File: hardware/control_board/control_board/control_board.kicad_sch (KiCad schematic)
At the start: 5 parts, among them J1 Conn_02x08_Counter_Clockwise, J3 USB_B

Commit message: feat：EEPROM原理图
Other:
- moved on the sheet: D2
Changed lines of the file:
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@@
 	(wire
 		(pts
-			(xy 55.88 29.21) (xy 55.88 30.48)
+			(xy 45.72 29.21) (xy 45.72 30.48)
 		)
 		(stroke
@@
 	(wire
 		(pts
-			(xy 55.88 55.88) (xy 55.88 58.42)
+			(xy 45.72 55.88) (xy 45.72 58.42)
 		)
 		(stroke
@@
 	(wire
 		(pts
-			(xy 27.94 43.18) (xy 43.18 43.18)
+			(xy 17.78 43.18) (xy 33.02 43.18)
 		)
 		(stroke
@@
 	(wire
 		(pts
-			(xy 68.58 43.18) (xy 82.55 43.18)
+			(xy 58.42 43.18) (xy 72.39 43.18)
 		)
 		(stroke
@@
 	)
 	(label "USB_D.USB_D+"
-		(at 27.94 43.18 0)
+		(at 17.78 43.18 0)
 		(effects
 			(font
@@
 	)
 	(label "USB_D.USB_D-"
-		(at 68.58 43.18 0)
+		(at 58.42 43.18 0)
 		(effects
 			(font
@@
 	(symbol
 		(lib_id "power:VBUS")
-		(at 55.88 29.21 0)
+		(at 45.72 29.21 0)
 		(unit 1)
 		(body_style 1)
@@
 		(fields_autoplaced yes)
 		(property "Reference" "#PWR021"
-			(at 55.88 33.02 0)
+			(at 45.72 33.02 0)
 			(hide yes)
 			(show_name no)
@@
 		)
 		(property "Value" "VBUS"
-			(at 55.88 24.13 0)
+			(at 45.72 24.13 0)
 			(show_name no)
 			(do_not_autoplace no)
@@
 		)
 		(property "Footprint" ""
-			(at 55.88 29.21 0)
+			(at 45.72 29.21 0)
 			(hide yes)
 			(show_name no)
@@
 		)
 		(property "Datasheet" ""
-			(at 55.88 29.21 0)
+			(at 45.72 29.21 0)
 			(hide yes)
 			(show_name no)
@@
 		)
 		(property "Description" "Power symbol creates a global label with name \"VBUS\""
-			(at 55.88 29.21 0)
+			(at 45.72 29.21 0)
 			(hide yes)
 			(show_name no)
@@
 	(symbol
 		(lib_id "Power_Protection:PRTR5V0U2X")
-		(at 55.88 43.18 0)
+		(at 45.72 43.18 0)
 		(unit 1)
 		(body_style 1)
@@
 		(dnp no)
 		(property "Reference" "D2"
-			(at 65.532 30.988 0)
+			(at 55.372 30.988 0)
 			(show_name no)
 			(do_not_autoplace no)
@@
 		)
 		(property "Value" "PRTR5V0U2X"
-			(at 65.532 33.528 0)
+			(at 55.372 33.528 0)
 			(show_name no)
 			(do_not_autoplace no)
@@
 		)
 		(property "Footprint" "Package_TO_SOT_SMD:SOT-143"
-			(at 57.404 43.18 0)
+			(at 47.244 43.18 0)
 			(hide yes)
 			(show_name no)
@@
 		)
 		(property "Datasheet" "https://assets.nexperia.com/documents/data-sheet/PRTR5V0U2X.pdf"
-			(at 57.404 43.18 0)
+			(at 47.244 43.18 0)
 			(hide yes)
 			(show_name no)
@@
 		)
 		(property "Description" "Ultra low capacitance double rail-to-rail ESD protection diode, SOT-143"
-			(at 55.88 43.18 0)
+			(at 45.72 43.18 0)
 			(hide yes)
 			(show_name no)
@@
 		)
 		(property "KLC_S3.3" ""
-			(at 55.88 43.18 0)
+			(at 45.72 43.18 0)
 			(hide yes)
 			(show_name no)
@@
 		)
 		(property "KLC_S4.1" ""
-			(at 55.88 43.18 0)
+			(at 45.72 43.18 0)
 			(hide yes)
 			(show_name no)
@@
 	(symbol
 		(lib_id "power:GND")
-		(at 55.88 58.42 0)
+		(at 45.72 58.42 0)
 		(unit 1)
 		(body_style 1)
@@
 		(fields_autoplaced yes)
 		(property "Reference" "#PWR020"
-			(at 55.88 64.77 0)
+			(at 45.72 64.77 0)
 			(hide yes)
 			(show_name no)
@@
 		)
 		(property "Value" "GND"
-			(at 55.88 63.5 0)
+			(at 45.72 63.5 0)
 			(show_name no)
 			(do_not_autoplace no)
@@
 		)
 		(property "Footprint" ""
-			(at 55.88 58.42 0)
+			(at 45.72 58.42 0)
 			(hide yes)
 			(show_name no)
@@
 		)
 		(property "Datasheet" ""
-			(at 55.88 58.42 0)
+			(at 45.72 58.42 0)
 			(hide yes)
 			(show_name no)
@@
 		)
 		(property "Description" "Power symbol creates a global label with name \"GND\" , ground"
-			(at 55.88 58.42 0)
-			(hide yes)
-			(show_name no)
+			(at 45.72 58.42 0)
+			(hide yes)
+			(show_name no)

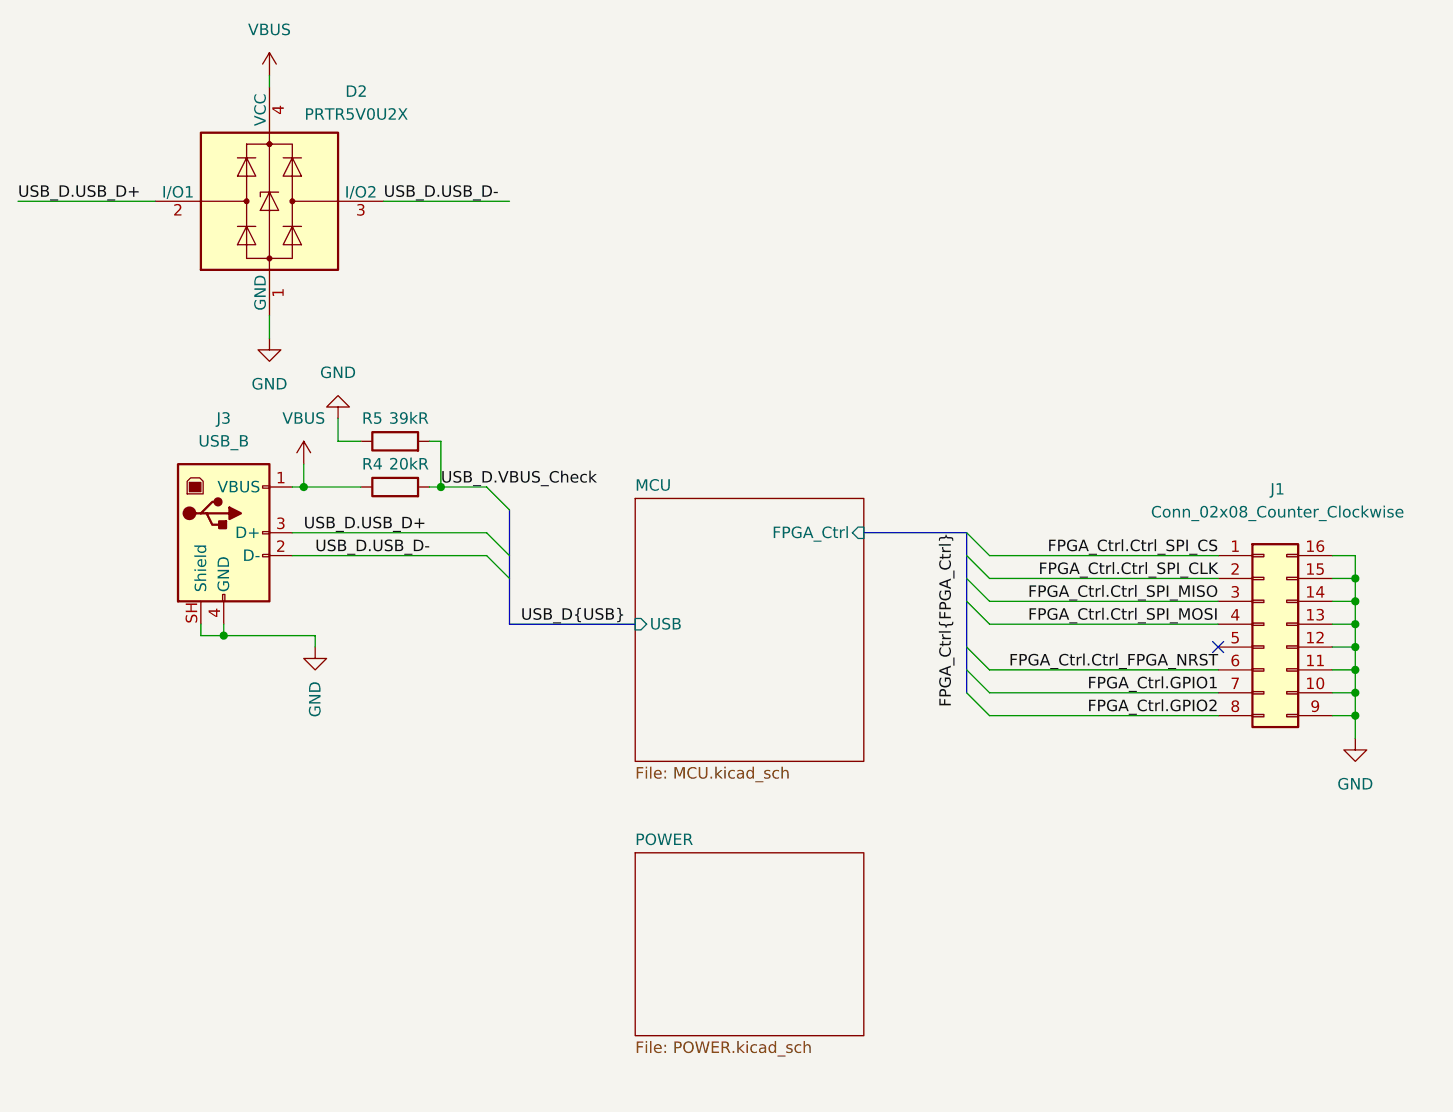
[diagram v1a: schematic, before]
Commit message: debug：蜂鸣器驱动电路；debug LED；电源输出排针
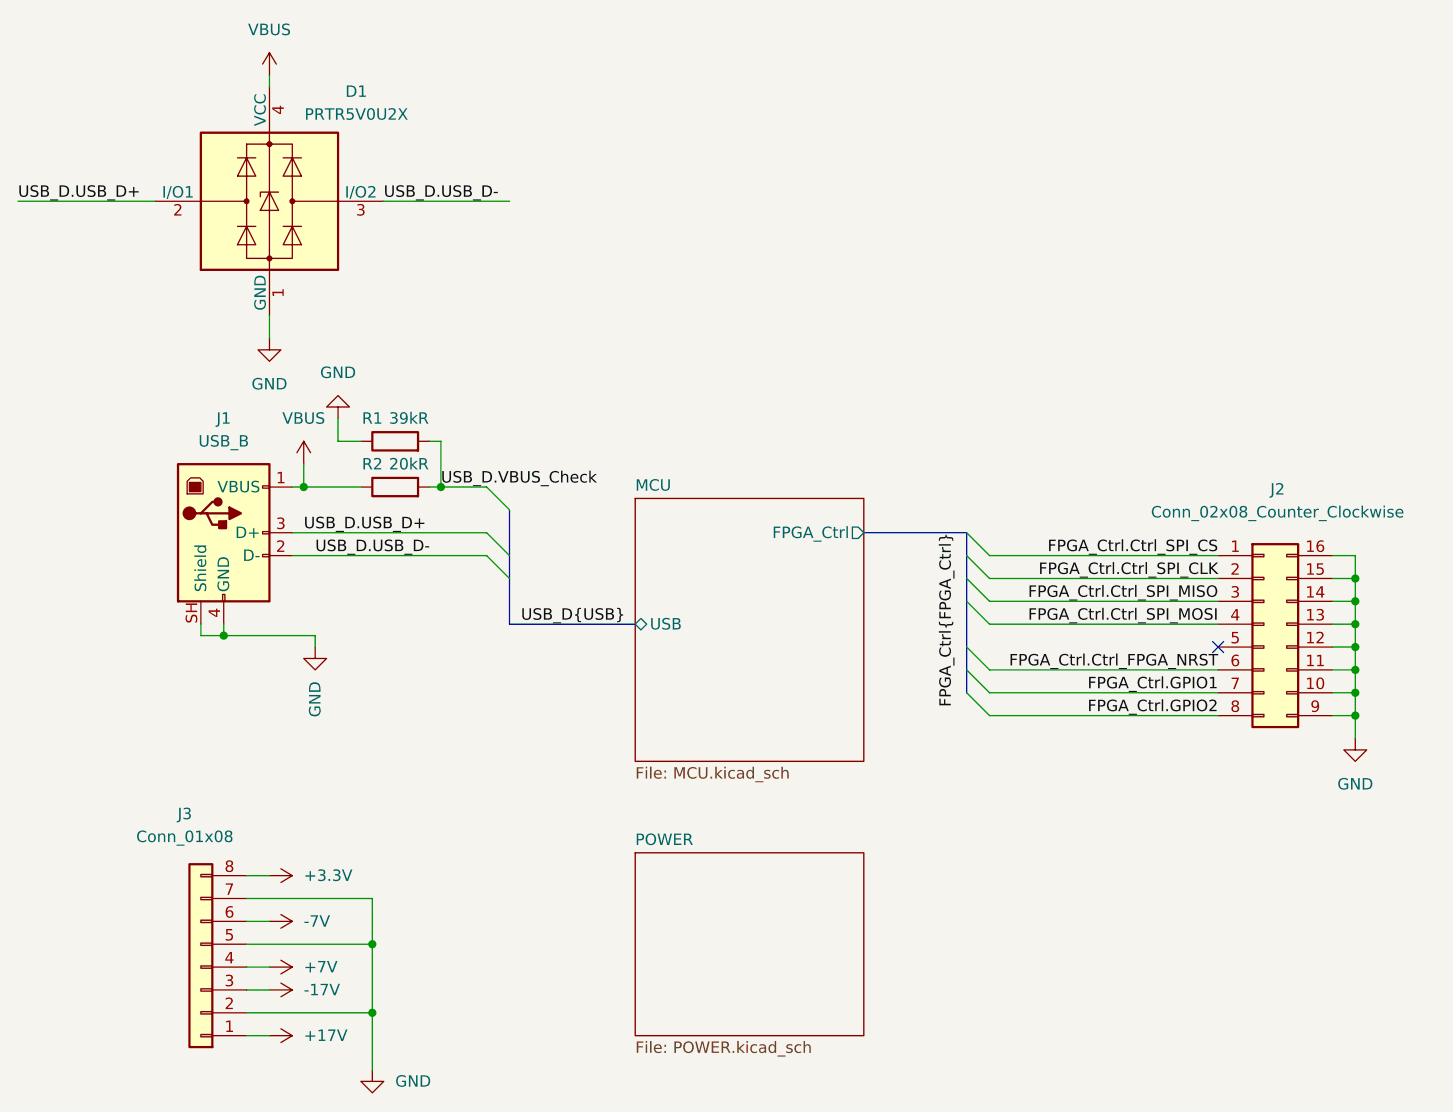
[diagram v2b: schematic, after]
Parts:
- added J3: Conn_01x08, Connector_JST:JST_VH_B8P-VH_1x08_P3.96mm_Vertical, symbol Connector_Generic:Conn_01x08
- renumbered D2 to D1, J3 to J1, J1 to J2, R5 to R1, R4 to R2
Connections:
- net GND: now also J3.2 (Pin_2), J3.5 (Pin_5), J3.7 (Pin_7)
- new net +17V: J3.1 (Pin_1)
- new net +3.3V: J3.8 (Pin_8)
- new net +7V: J3.4 (Pin_4)
- new net -17V: J3.3 (Pin_3)
- new net -7V: J3.6 (Pin_6)

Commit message: feat：根据PCB微调原理图
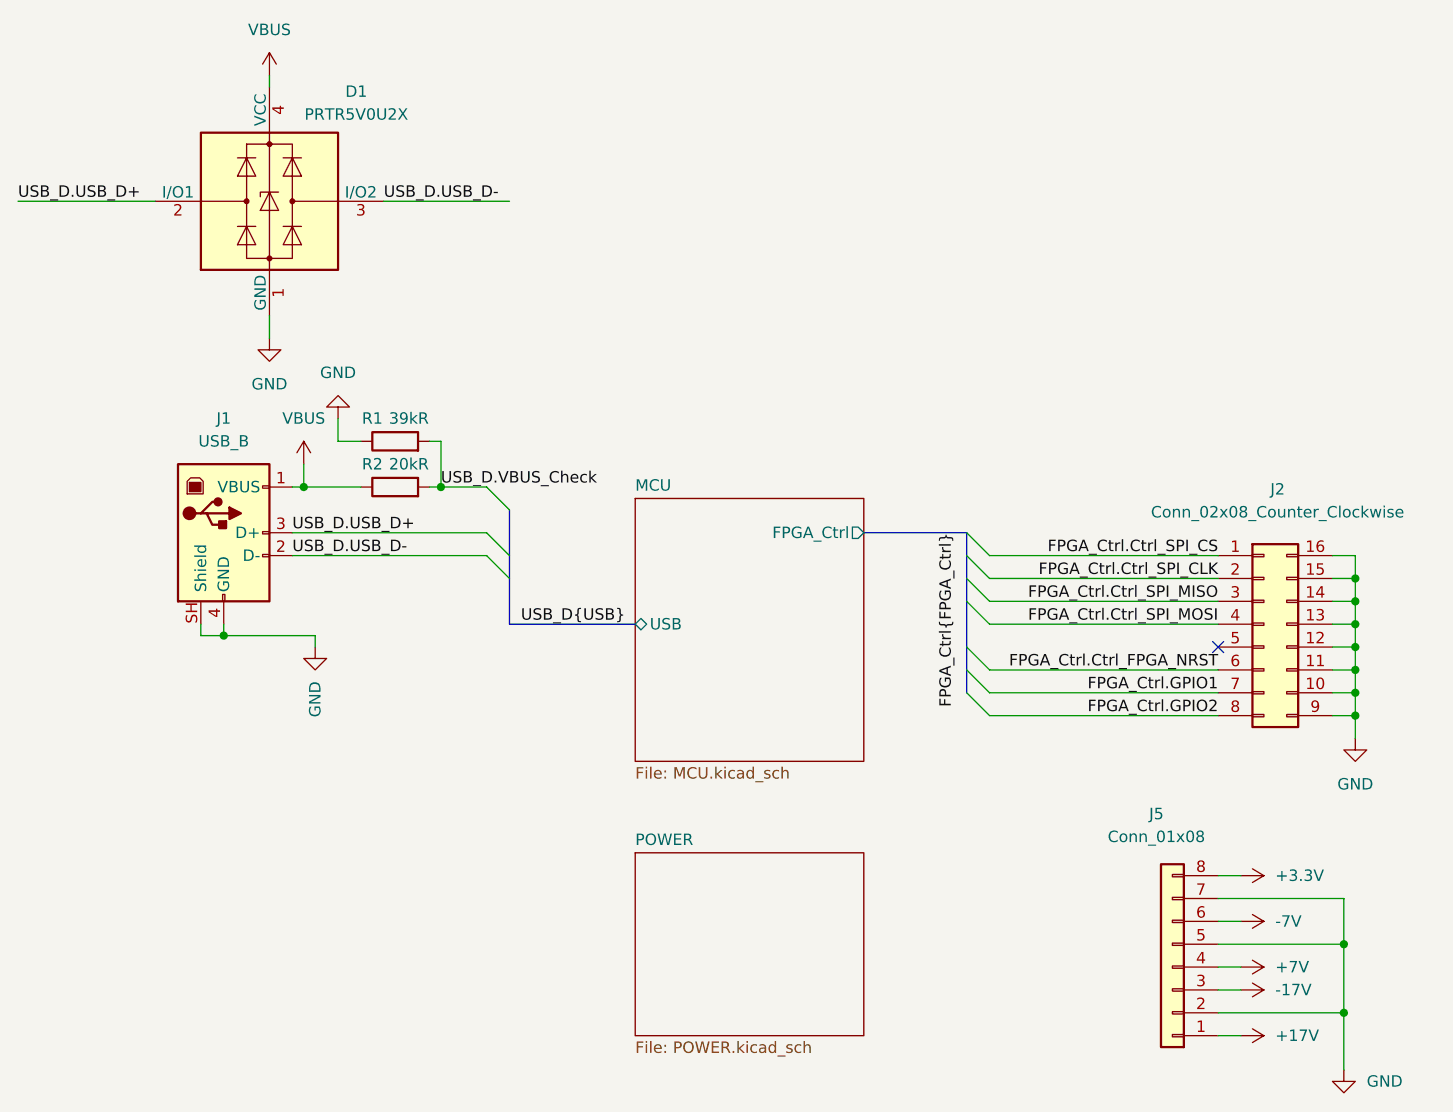
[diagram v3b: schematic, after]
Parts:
- renumbered J3 to J5
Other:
- moved on the sheet: J5
